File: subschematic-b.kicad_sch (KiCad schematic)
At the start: 0 parts

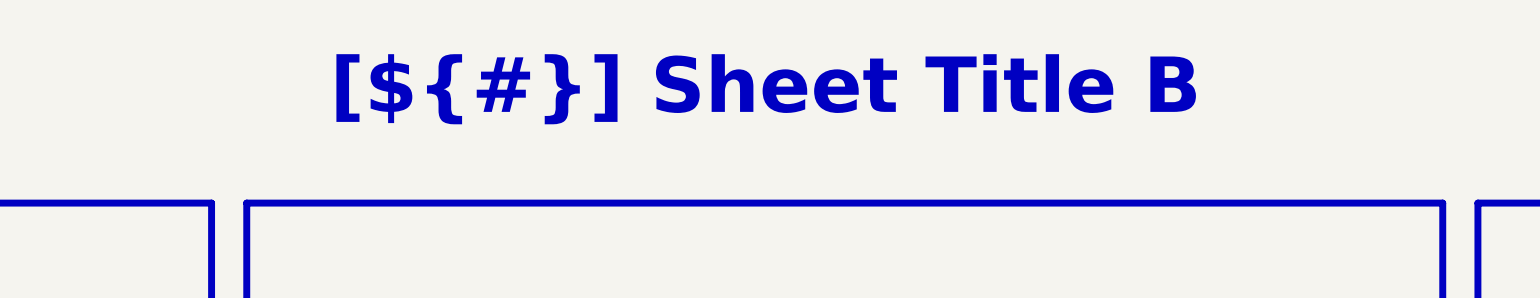
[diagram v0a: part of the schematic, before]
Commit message: feat: convert template to Boardwright
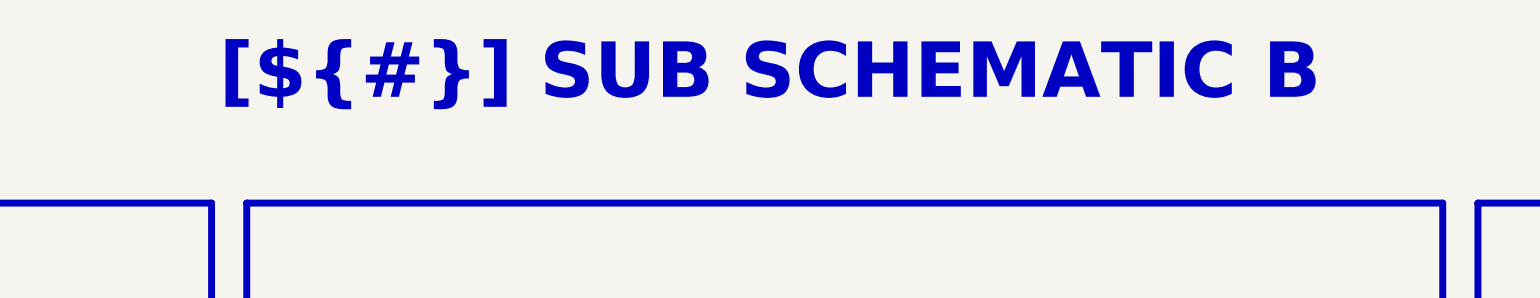
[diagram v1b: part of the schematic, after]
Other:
- title: Sheet Title B -> SUB SCHEMATIC B
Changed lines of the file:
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@@
 	(paper "A3")
 	(title_block
-		(title "Sheet Title B")
+		(title "SUB SCHEMATIC B")
 		(date "2025-01-12")
 		(rev "${REVISION}")
@@
 	(text_box "[${#}] ${TITLE}"
 		(exclude_from_sim no)
-		(at 140.97 15 0)
-		(size 147.32 15)
+		(at 20.32 10.16 0)
+		(size 389.89 20.32)
 		(margins 5.9999 5.9999 5.9999 5.9999)
 		(stroke

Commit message: feat: prepare Boardwright template workflow
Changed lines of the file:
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@@
 	(rectangle
 		(start 317.5 39.37)
-		(end 373.38 240.03)
+		(end 373.38 205.74)
 		(stroke
 			(width 1)
@@
 	)
 	(rectangle
-		(start 45.72 210.82)
-		(end 134.62 240.03)
-		(stroke
-			(width 1)
-			(type default)
-			(color 200 200 200 1)
-		)
-		(fill
-			(type none)
-		)
-	)
-	(rectangle
 		(start 229.87 186.69)
 		(end 312.42 205.74)
@@
 	)
 	(rectangle
-		(start 139.7 210.82)
-		(end 224.79 240.03)
-		(stroke
-			(width 1)
-			(type default)
-			(color 200 200 200 1)
-		)
-		(fill
-			(type none)
-		)
-	)
-	(rectangle
 		(start 45.72 39.37)
 		(end 134.62 167.64)
@@
 		)
 	)
-	(rectangle
-		(start 229.87 210.82)
-		(end 312.42 240.03)
-		(stroke
-			(width 1)
-			(type default)
-			(color 200 200 200 1)
-		)
-		(fill
-			(type none)
-		)
-	)
 	(text "Flexible I/O worked examples"
 		(exclude_from_sim no)
@@
 		(at 46.99 194.31 0)
 		(size 86.36 9.525)
-		(margins 1.9049 1.9049 1.9049 1.9049)
-		(stroke
-			(width -0.0001)
-			(type default)
-		)
-		(fill
-			(type none)
-		)
-		(effects
-			(font
-				(size 2.54 2.54)
-				(thickness 0.508)
-				(bold yes)
-				(color 162 22 34 1)
-			)
-			(justify bottom)
-		)
-	)
-	(text_box "Block Description"
-		(exclude_from_sim no)
-		(at 140.97 228.6 0)
-		(size 82.55 9.525)
 		(margins 1.9049 1.9049 1.9049 1.9049)
 		(stroke
@@
 		)
 	)
-	(text_box "Block Description"
-		(exclude_from_sim no)
-		(at 46.99 228.6 0)
-		(size 86.36 9.525)
-		(margins 1.9049 1.9049 1.9049 1.9049)
-		(stroke
-			(width -0.0001)
-			(type default)
-		)
-		(fill
-			(type none)
-		)
-		(effects
-			(font
-				(size 2.54 2.54)
-				(thickness 0.508)
-				(bold yes)
-				(color 162 22 34 1)
-			)
-			(justify bottom)
-		)
-	)
 	(text_box "DESIGN NOTE:\nblabla"
 		(exclude_from_sim no)
@@
 		)
 	)
-	(text_box "Block Description"
-		(exclude_from_sim no)
-		(at 231.14 228.6 0)
-		(size 80.01 9.525)
-		(margins 1.9049 1.9049 1.9049 1.9049)
-		(stroke
-			(width -0.0001)
-			(type default)
-		)
-		(fill
-			(type none)
-		)
-		(effects
-			(font
-				(size 2.54 2.54)
-				(thickness 0.508)
-				(bold yes)
-				(color 162 22 34 1)
-			)
-			(justify bottom)
-		)
-	)
 	(text_box "LAYOUT NOTE:\nblabla"
 		(exclude_from_sim no)
@@
 	(text_box "Block Description"
 		(exclude_from_sim no)
-		(at 231.14 194.31 0)
+		(at 231.14 194.945 0)
 		(size 80.01 9.525)
 		(margins 1.9049 1.9049 1.9049 1.9049)
@@
 		(effects
 			(font
-				(size 2.54 2.54)
-				(thickness 0.508)
-				(bold yes)
-				(color 162 22 34 1)
-			)
-			(justify bottom)
-		)
-	)
-	(text_box "Block Description"
-		(exclude_from_sim no)
-		(at 318.77 228.6 0)
-		(size 53.34 9.525)
-		(margins 1.9049 1.9049 1.9049 1.9049)
-		(stroke
-			(width -0.0001)
-			(type default)
-		)
-		(fill
-			(type none)
-		)
-		(effects
-			(font
-				(face "Times New Roman")
 				(size 2.54 2.54)
 				(thickness 0.508)
@@
 	(text_box "Block Description"
 		(exclude_from_sim no)
-		(at 140.97 194.31 0)
+		(at 140.97 194.945 0)
 		(size 82.55 9.525)
 		(margins 1.9049 1.9049 1.9049 1.9049)
 		(stroke
+			(width -0.0001)
+			(type default)
+		)
+		(fill
+			(type none)
+		)
+		(effects
+			(font
+				(size 2.54 2.54)
+				(thickness 0.508)
+				(bold yes)
+				(color 162 22 34 1)
+			)
+			(justify bottom)
+		)
+	)
+	(text_box "Block Description"
+		(exclude_from_sim no)
+		(at 318.77 195.58 0)
+		(size 53.34 9.525)
+		(margins 1.9049 1.9049 1.9049 1.9049)
+		(stroke
